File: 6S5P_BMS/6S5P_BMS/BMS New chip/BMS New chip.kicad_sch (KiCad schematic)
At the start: 3 parts, among them J1 Screw_Terminal_01x02, U1 MP2793DFP-0002-T, U2 MPF42792DRT-0B-0000-P

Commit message: saved again
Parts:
- added BT1: Battery_Cell, symbol Device:Battery_Cell
- added C1: 1u, rsx_capacitors:C_0805_2012Metric, symbol rsx_Capacitors:1u
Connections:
- net 3V3: now also J1.1 (Pin_1), C1.2
- net GND: now reaches U1.23 (AGND)
- net GND: now also J1.2 (Pin_2), C1.1
- net at U1.45 (TOP): now also BT1.1 (+)
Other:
- moved on the sheet: J1

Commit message: added to the mpf42792 chip
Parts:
- added C2: 2.2u, Capacitor_SMD:C_0603_1608Metric, symbol rsx_Capacitors:2u2_0603
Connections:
- net GND: now also C2.2
- net +3.3V: now reaches U2.10 (VDD)
- net +3.3V: now also C2.1

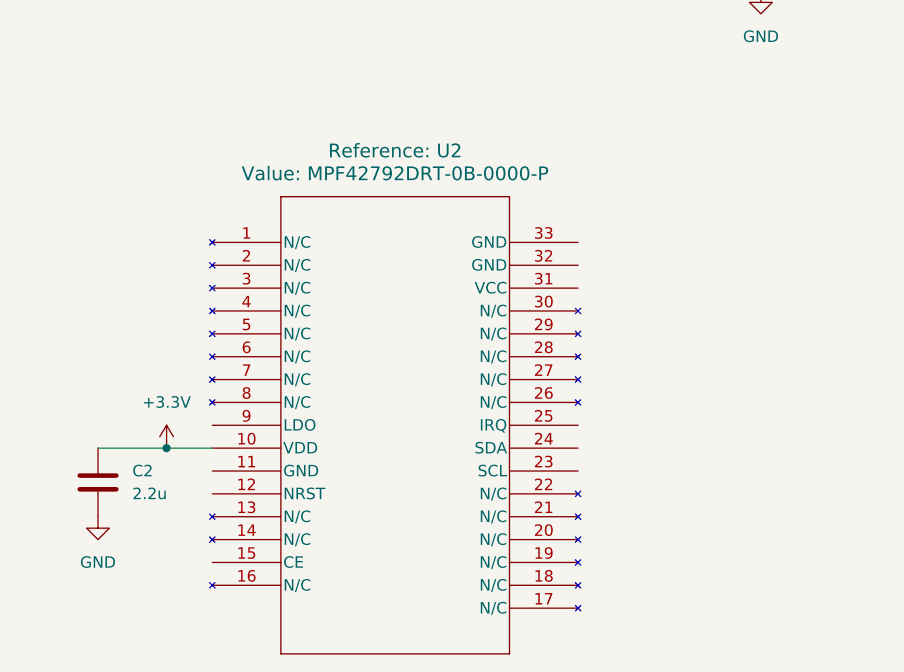
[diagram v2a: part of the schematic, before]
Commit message: added what i could for the mpf42792 ic chip
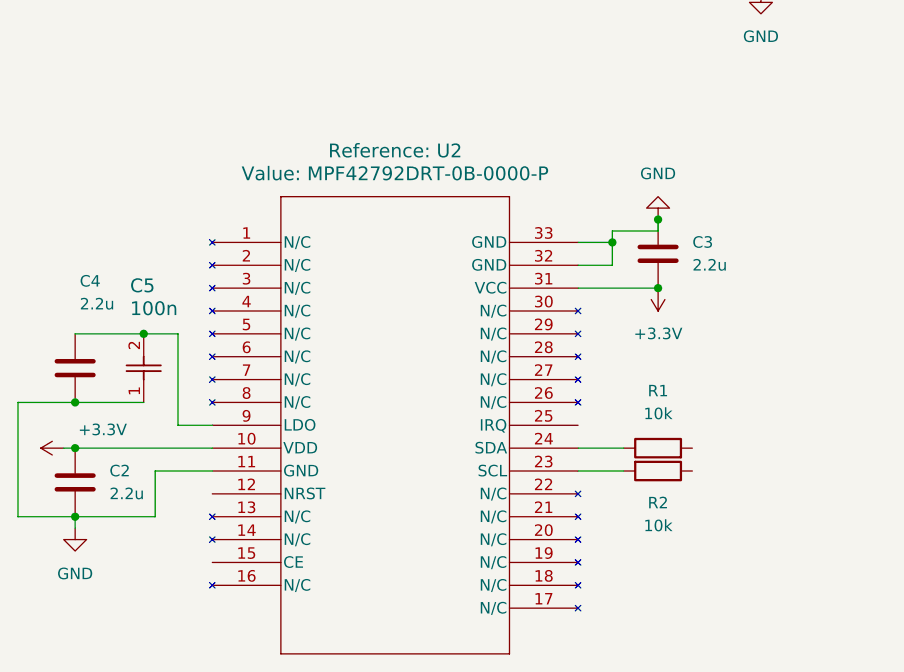
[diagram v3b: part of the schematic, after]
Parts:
- added C3, C4: 2.2u, Capacitor_SMD:C_0603_1608Metric, symbol rsx_Capacitors:2u2_0603
- added C5: 100n, Capacitor_SMD:C_0603_1608Metric, symbol rsx_Capacitors:100n
- added R1, R2: 10k, rsx_resistors:R_0603_1608Metric, symbol rsx_Resistors:10k
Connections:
- net +3.3V: now also U2.31 (VCC), C3.2
- net GND: now also U2.11 (GND), U2.32 (GND), U2.33 (GND), C3.1, C4.2, C5.1
- net at U2.23 (SCL): now also R2.2
- net at U2.24 (SDA): now also R1.1
- net at U2.9 (LDO): now also C4.1, C5.2
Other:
- moved on the sheet: C2

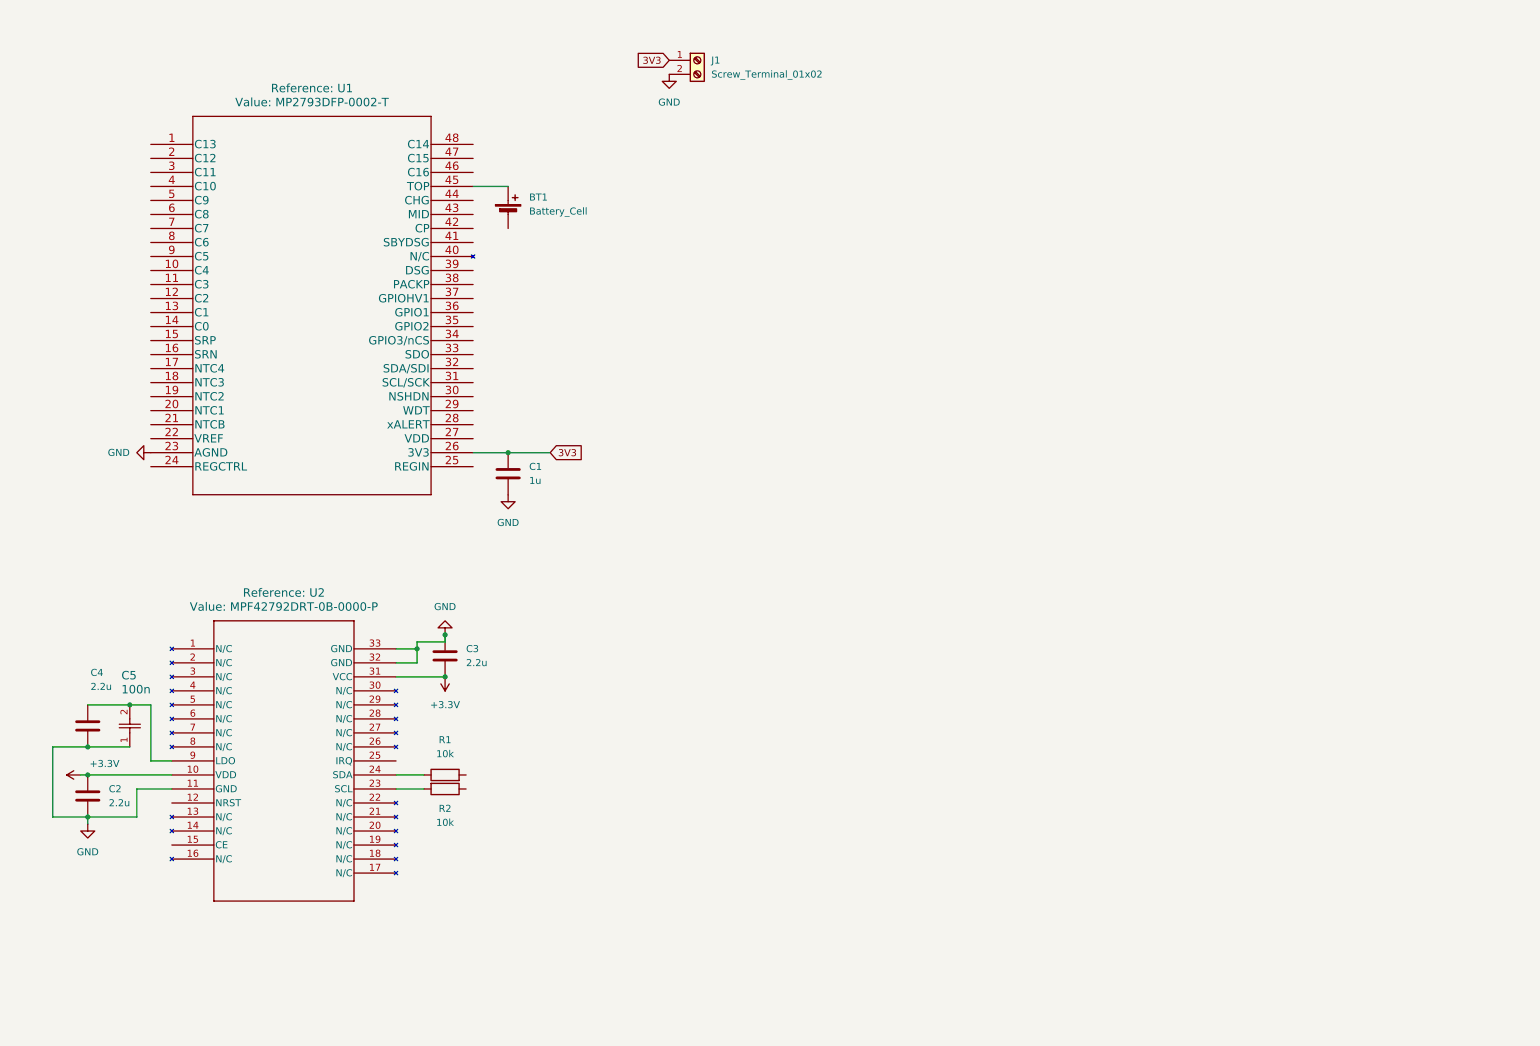
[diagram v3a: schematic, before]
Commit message: Implemented the external balancer circuit on the new bms chip and fully connected the pins of MP42792
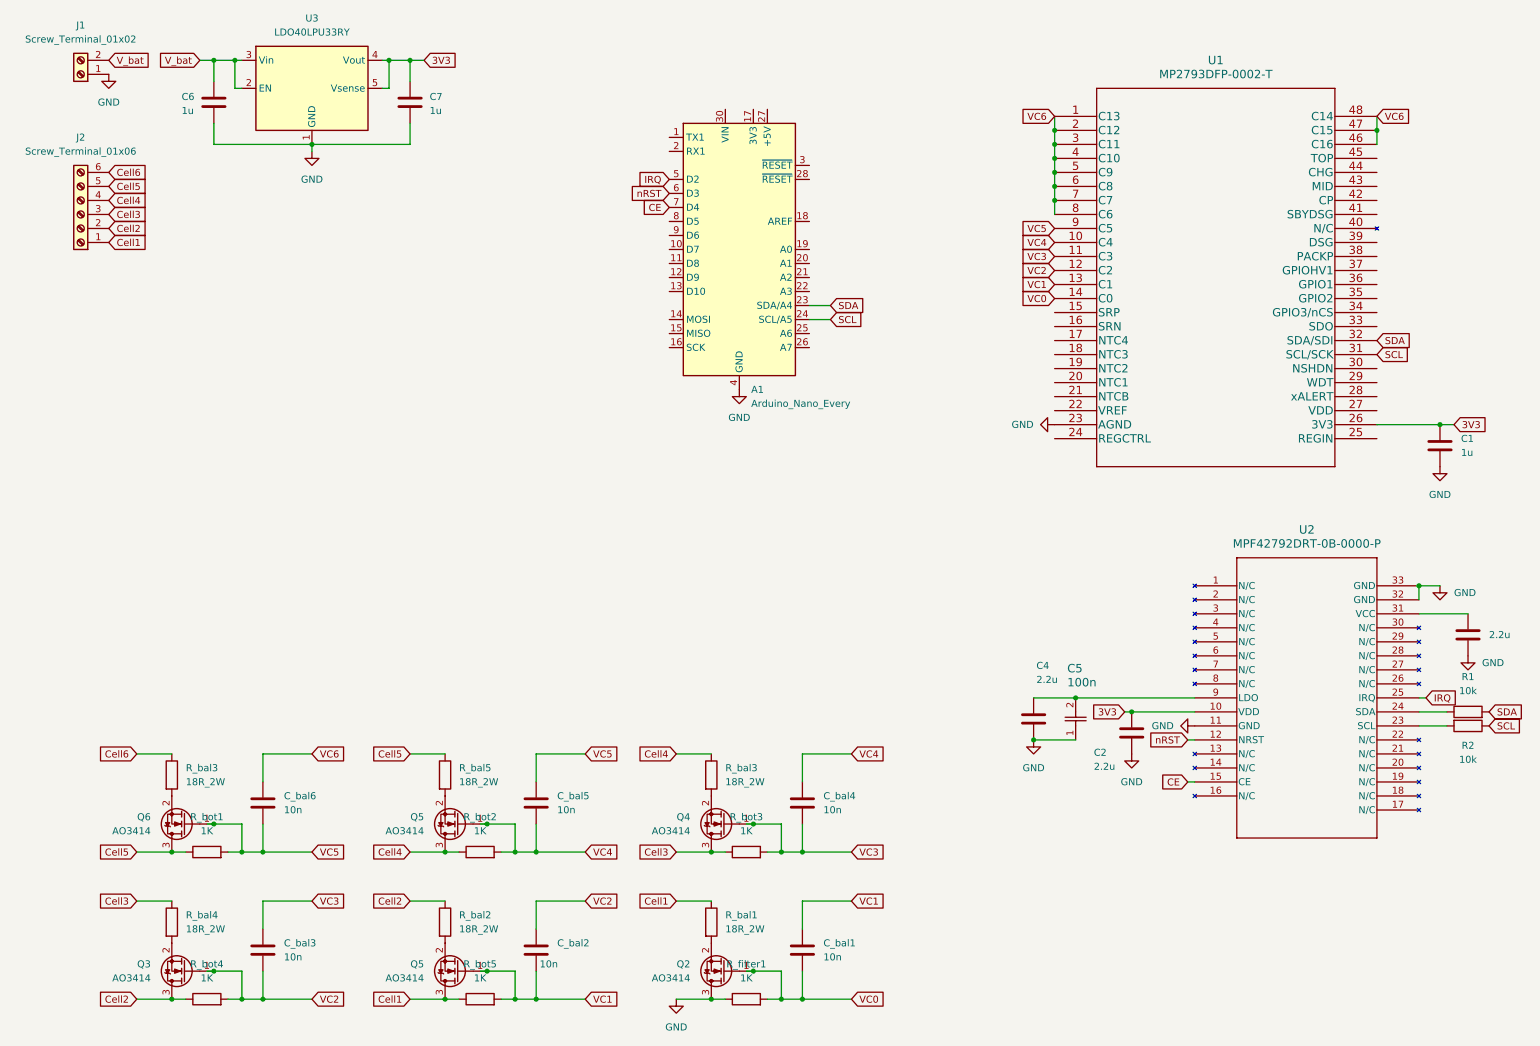
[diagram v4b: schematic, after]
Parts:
- removed BT1: Battery_Cell, symbol Device:Battery_Cell
- added A1: Arduino_Nano_Every, Module:Arduino_Nano, symbol rsx_Modules:Arduino_Nano_Every
- added C6, C7: 1u, rsx_capacitors:C_0805_2012Metric, symbol rsx_Capacitors:1u
- added C_bal1, C_bal2, C_bal3, C_bal4, C_bal5, C_bal6: 10n, rsx_capacitors:C_0603_1608Metric, symbol rsx_Capacitors:10n
- added J2: Screw_Terminal_01x06, symbol Connector:Screw_Terminal_01x06
- added Q2, Q3, Q4, Q5 (x2), Q6: AO3414, Package_TO_SOT_SMD:SOT-23, symbol rsx_Transistors:AO3414
- added R_bal1, R_bal2, R_bal3 (x2), R_bal4, R_bal5: 18R_2W, rsx_resistors:R_Axial_DIN0516_L15.5mm_D5.0mm_P20.32mm_Horizontal, symbol rsx_Resistors:18R_2W
- added R_bot1, R_bot2, R_bot3, R_bot4, R_bot5, R_filter1: 1K, rsx_resistors:R_0603_1608Metric, symbol rsx_Resistors:1K
- added U3: LDO40LPU33RY, Package_DFN_QFN:DFN-6-1EP_3x3mm_P0.95mm_EP1.7x2.6mm, symbol Regulator_Linear:LDO40LPU33RY
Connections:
- net 3V3: now also C2.1, U2.10 (VDD), C7.1, U3.4 (Vout), U3.5 (Vsense); no longer J1.1 (Pin_1)
- net GND: now also J1.1 (Pin_1), A1.29 (GND), A1.4 (GND), C6.2, C7.2, Q2.3 (D), R_filter1.1, U3.1 (GND), U3.7 (GND); no longer J1.2 (Pin_2)
- net VC6: now reaches U1.1 (C13)
- net VC6: now also U1.2 (C12), U1.3 (C11), U1.4 (C10), U1.46 (C16), U1.47 (C15), U1.48 (C14), U1.5 (C9), U1.6 (C8), U1.7 (C7), U1.8 (C6), C_bal6.1
- net VC4: now reaches U1.10 (C4)
- net VC4: now also C_bal4.1, C_bal5.2, Q5.1 (G), R_bot2.2
- net VC3: now reaches U1.11 (C3)
- net VC3: now also C_bal3.1, C_bal4.2, Q4.1 (G), R_bot3.2
- net VC2: now reaches U1.12 (C2)
- net VC2: now also C_bal2.1, C_bal3.2, Q3.1 (G), R_bot4.2
- net VC1: now reaches U1.13 (C1)
- net VC1: now also C_bal1.1, C_bal2.2, Q5.1 (G), R_bot5.2
- net VC0: now reaches U1.14 (C0)
- net VC0: now also C_bal1.2, Q2.1 (G), R_filter1.2
- net SCL: now reaches U1.31 (SCL/SCK)
- net SCL: now also R2.1, A1.24 (SCL/A5)
- net SDA: now reaches U1.32 (SDA/SDI)
- net SDA: now also R1.2, A1.23 (SDA/A4)
- net VC5: now reaches U1.9 (C5)
- net VC5: now also C_bal5.1, C_bal6.2, Q6.1 (G), R_bot1.2
- net nRST: now reaches U2.12 (NRST)
- net nRST: now also A1.6 (D3)
- net CE: now reaches U2.15 (CE)
- net CE: now also A1.7 (D4)
- net IRQ: now reaches U2.25 (IRQ)
- net IRQ: now also A1.5 (D2)
- net +3.3V: no longer names the net of C3.2, U2.31 (VCC)
- net +3.3V: no longer C2.1, U2.10 (VDD)
- new net: Q6.2 (S), R_bal3.2
- new net: Q4.2 (S), R_bal3.2
- new net: Q5.2 (S), R_bal2.2
- new net: Q5.2 (S), R_bal5.2
- new net: Q3.2 (S), R_bal4.2
- new net: Q2.2 (S), R_bal1.2
- new net Cell1: J2.1 (Pin_1), Q5.3 (D), R_bal1.1, R_bot5.1
- new net Cell2: J2.2 (Pin_2), Q3.3 (D), R_bal2.1, R_bot4.1
- new net Cell3: J2.3 (Pin_3), Q4.3 (D), R_bal4.1, R_bot3.1
- new net Cell4: J2.4 (Pin_4), Q5.3 (D), R_bal3.1, R_bot2.1
- new net Cell5: J2.5 (Pin_5), Q6.3 (D), R_bal5.1, R_bot1.1
- new net Cell6: J2.6 (Pin_6), R_bal3.1
- new net V_bat: C6.1, J1.2 (Pin_2), U3.2 (EN), U3.3 (Vin)
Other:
- moved on the sheet: C1, C2, C4, C5, J1, R1, R2, U1, U2
